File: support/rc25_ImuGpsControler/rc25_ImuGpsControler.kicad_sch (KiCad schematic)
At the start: 3 parts, among them J1 IMU_6pin, J2 GPS_6pin, U1 RP2040-Zero

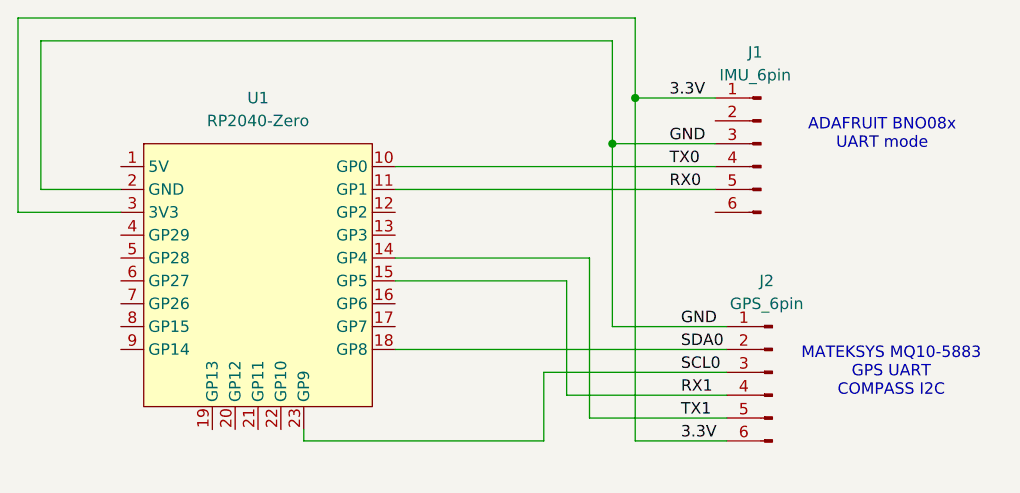
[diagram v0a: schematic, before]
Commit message: Updated IMU GPS cntroller board schematic movint the GPS serial port to different pins
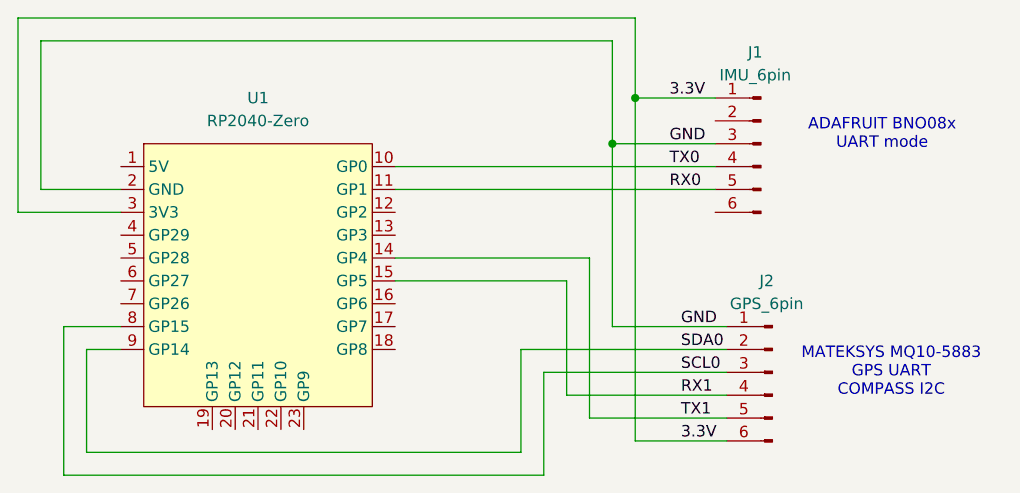
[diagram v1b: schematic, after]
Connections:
- net SCL0: now also U1.8 (GP15); no longer U1.23 (GP9)
- net SDA0: now also U1.9 (GP14); no longer U1.18 (GP8)
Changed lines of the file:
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@@
 	(wire
 		(pts
-			(xy 144.78 115.57) (xy 181.61 115.57)
-		)
-		(stroke
-			(width 0)
-			(type default)
-		)
-	)
-	(wire
-		(pts
-			(xy 161.29 118.11) (xy 161.29 125.73)
+			(xy 107.95 113.03) (xy 107.95 129.54)
+		)
+		(stroke
+			(width 0)
+			(type default)
+		)
+	)
+	(wire
+		(pts
+			(xy 161.29 118.11) (xy 161.29 129.54)
 		)
 		(stroke
@@
 	(wire
 		(pts
+			(xy 107.95 113.03) (xy 114.3 113.03)
+		)
+		(stroke
+			(width 0)
+			(type default)
+		)
+	)
+	(wire
+		(pts
 			(xy 102.87 100.33) (xy 114.3 100.33)
 		)
@@
 	(wire
 		(pts
-			(xy 134.62 125.73) (xy 161.29 125.73)
+			(xy 158.75 115.57) (xy 158.75 127)
+		)
+		(stroke
+			(width 0)
+			(type default)
+		)
+	)
+	(wire
+		(pts
+			(xy 158.75 115.57) (xy 181.61 115.57)
 		)
 		(stroke
@@
 	(wire
 		(pts
-			(xy 134.62 125.73) (xy 134.62 124.46)
+			(xy 107.95 129.54) (xy 161.29 129.54)
 		)
 		(stroke
@@
 	(wire
 		(pts
+			(xy 110.49 115.57) (xy 114.3 115.57)
+		)
+		(stroke
+			(width 0)
+			(type default)
+		)
+	)
+	(wire
+		(pts
 			(xy 102.87 78.74) (xy 102.87 100.33)
 		)
@@
 	(wire
 		(pts
+			(xy 110.49 127) (xy 158.75 127)
+		)
+		(stroke
+			(width 0)
+			(type default)
+		)
+	)
+	(wire
+		(pts
 			(xy 144.78 97.79) (xy 180.34 97.79)
 		)
@@
 		)
 		(stroke
+			(width 0)
+			(type default)
+		)
+	)
+	(wire
+		(pts
+			(xy 110.49 115.57) (xy 110.49 127)
+		)
+		(stroke
